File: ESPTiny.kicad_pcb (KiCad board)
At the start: 2 copper layers, 33 x 26.4 mm, 18 parts, among them J1 Conn_01x10_Male, J2 Conn_01x10_Male, J3 Conn_01x04_Male, U1 ESP-01v090, U2 ATtiny84-20PU, U3 MCP1700-3302E_TO92

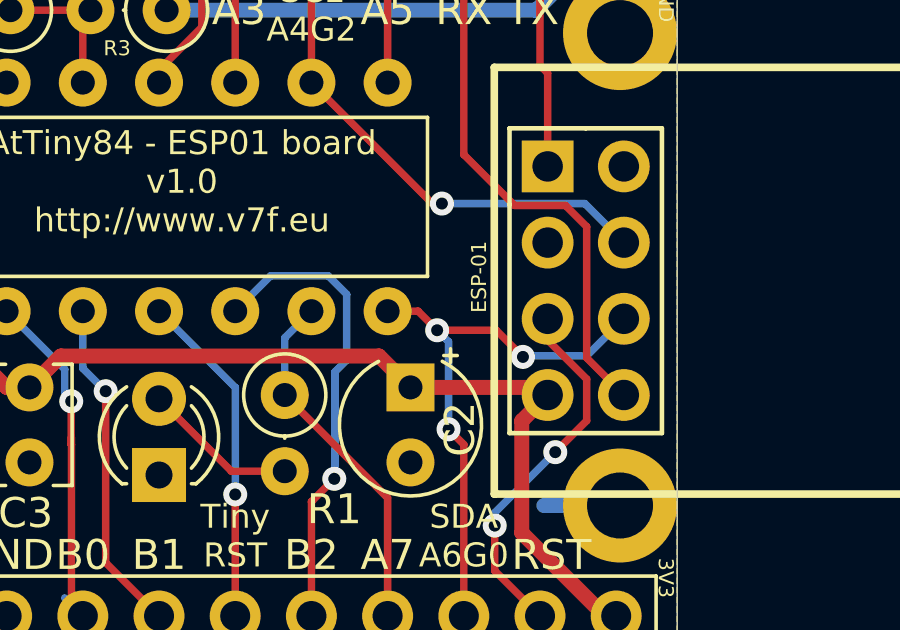
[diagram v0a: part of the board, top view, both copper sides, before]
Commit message: Fix ESP CH_PD to 3V3
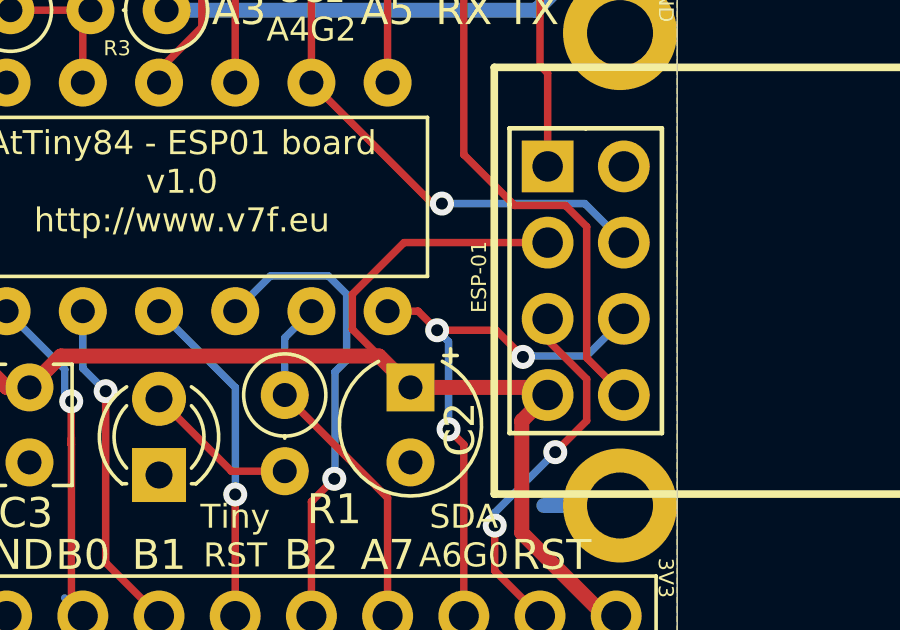
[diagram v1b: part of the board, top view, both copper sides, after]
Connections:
- U1 pad 3: GND -> +3V3
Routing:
- net +3V3: track 45.1 -> 56.2 mm

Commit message: Copper fill
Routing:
- net +3V3: track 56.2 -> 45.1 mm
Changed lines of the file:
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@@
     (thickness 1.6)
     (drawings 49)
-    (tracks 154)
+    (tracks 150)
     (zones 0)
     (modules 18)
@@
   (segment (start 43.942 61.722) (end 47.244 65.024) (width 0.5) (layer F.Cu) (net 2))
   (segment (start 43.942 60.706) (end 43.942 61.722) (width 0.5) (layer F.Cu) (net 2))
-  (segment (start 61.308999 55.466999) (end 63.246 57.404) (width 0.25) (layer F.Cu) (net 2))
-  (segment (start 61.308999 54.299999) (end 61.308999 55.466999) (width 0.25) (layer F.Cu) (net 2))
-  (segment (start 63.030998 52.578) (end 61.308999 54.299999) (width 0.25) (layer F.Cu) (net 2))
-  (segment (start 67.818 52.578) (end 63.030998 52.578) (width 0.25) (layer F.Cu) (net 2))
   (segment (start 43.528999 48.419001) (end 43.434 48.514) (width 0.25) (layer F.Cu) (net 3))
   (segment (start 43.022999 48.102999) (end 43.434 48.514) (width 0.5) (layer F.Cu) (net 3))
@@
   )
   (zone (net 2) (net_name +3V3) (layer F.Cu) (hatch edge 0.508)
+    (priority 1)
     (connect_pads (clearance 0.508))
     (min_thickness 0.254)

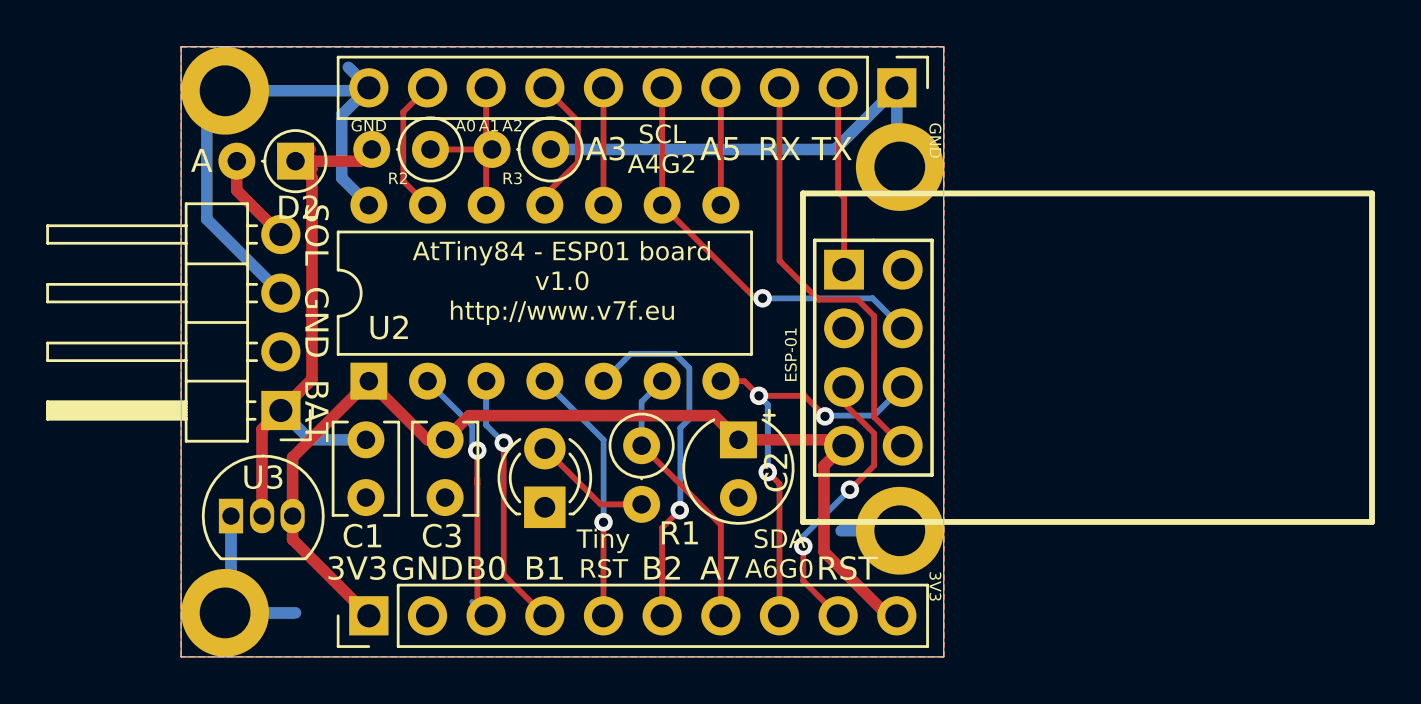
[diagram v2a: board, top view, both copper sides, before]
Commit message: Copper fill smaller clearance
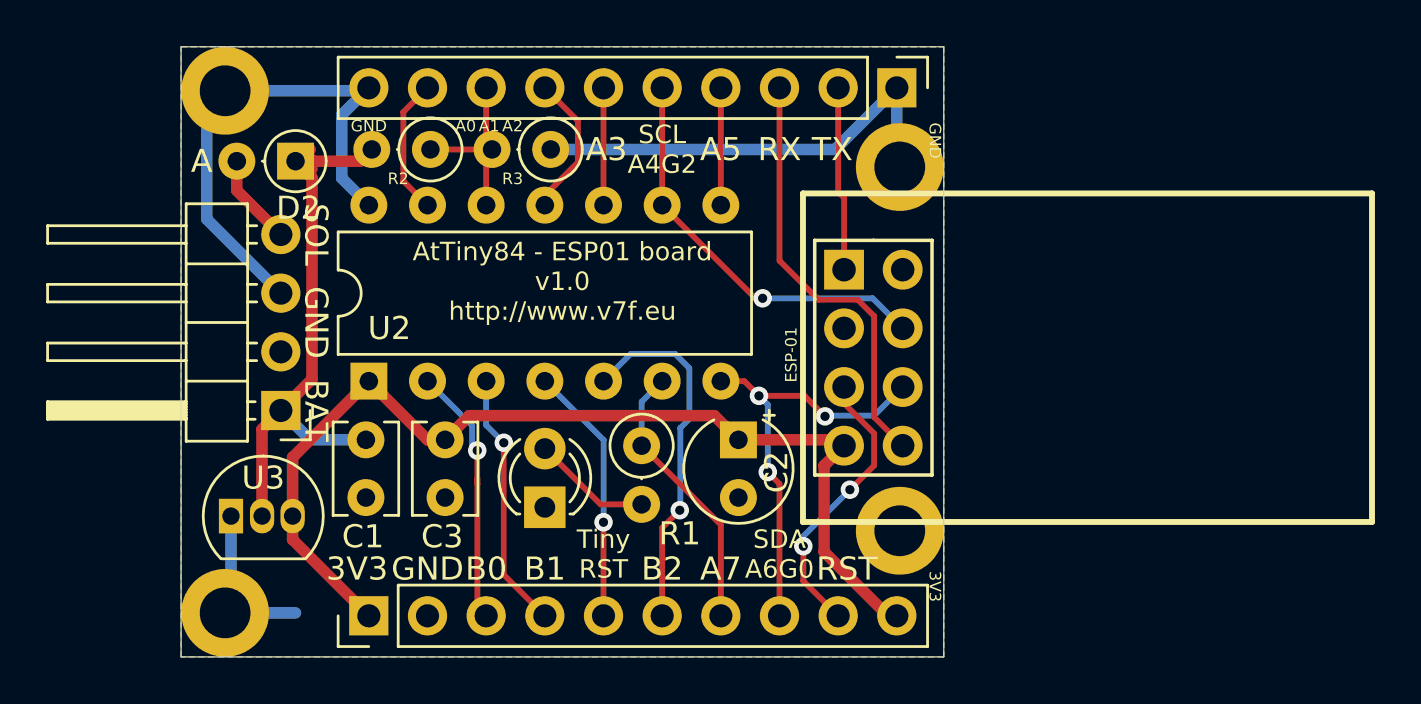
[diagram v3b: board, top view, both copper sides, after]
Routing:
- net GND: track 53.6 -> 49.8 mm
- net /B0: track 12.3 -> 11.4 mm
- removed copper zone on F.Cu, net (none)

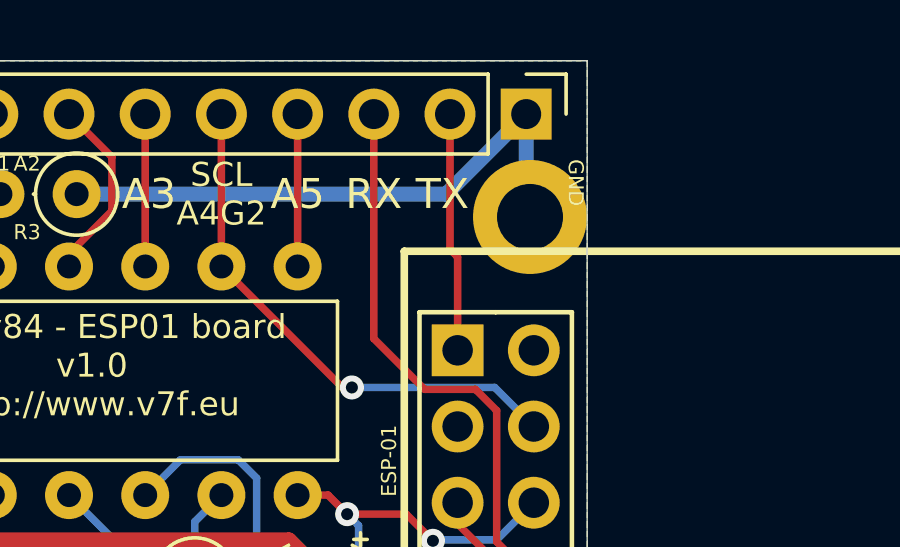
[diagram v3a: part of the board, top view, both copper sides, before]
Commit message: Copper fill smaller clearance: 0.27
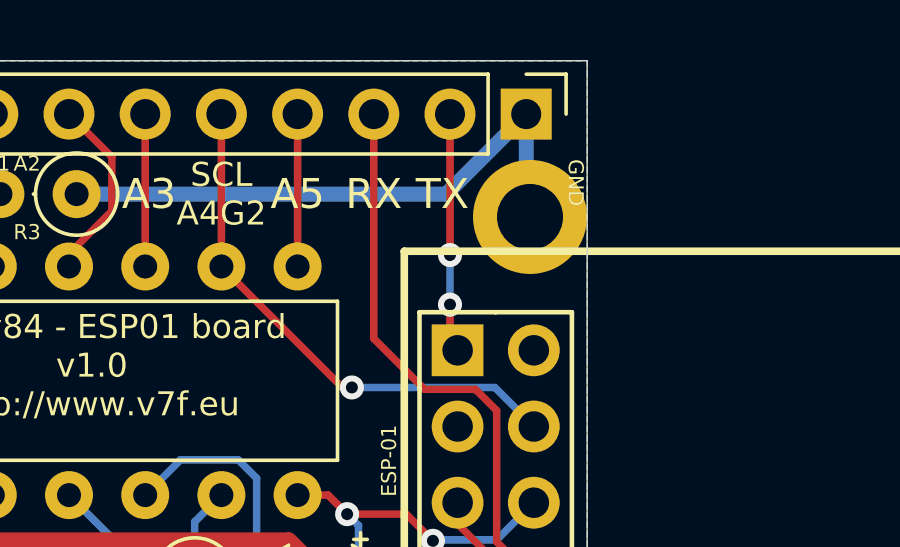
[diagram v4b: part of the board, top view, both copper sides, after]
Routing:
- net /TX: vias 0 -> 2
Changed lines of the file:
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@@
     (thickness 1.6)
     (drawings 49)
-    (tracks 147)
+    (tracks 150)
     (zones 0)
     (modules 18)
@@
     (last_trace_width 0.25)
     (trace_clearance 0.25)
-    (zone_clearance 0.29)
+    (zone_clearance 0.27)
     (zone_45_only no)
     (trace_min 0.25)
@@
   (segment (start 66.054401 61.580599) (end 66.054401 62.010167) (width 0.25) (layer B.Cu) (net 12))
   (segment (start 68.072 59.563) (end 66.054401 61.580599) (width 0.25) (layer B.Cu) (net 12))
-  (segment (start 67.564 46.674002) (end 67.564 42.164) (width 0.25) (layer F.Cu) (net 13) (status 20))
-  (segment (start 67.818 46.928002) (end 67.564 46.674002) (width 0.25) (layer F.Cu) (net 13))
-  (segment (start 67.818 50.038) (end 67.818 46.928002) (width 0.25) (layer F.Cu) (net 13) (status 10))
+  (via (at 67.564 46.863) (size 0.8) (drill 0.4) (layers F.Cu B.Cu) (net 13))
+  (via (at 67.564 48.514) (size 0.8) (drill 0.4) (layers F.Cu B.Cu) (net 13))
+  (segment (start 67.564 42.164) (end 67.564 46.863) (width 0.25) (layer F.Cu) (net 13))
+  (segment (start 67.564 49.784) (end 67.818 50.038) (width 0.25) (layer F.Cu) (net 13))
+  (segment (start 67.564 48.514) (end 67.564 49.784) (width 0.25) (layer F.Cu) (net 13))
+  (segment (start 67.564 46.863) (end 67.564 48.514) (width 0.25) (layer B.Cu) (net 13))
   (segment (start 69.119399 56.419399) (end 70.358 57.658) (width 0.25) (layer F.Cu) (net 14) (status 20))
   (segment (start 69.119399 52.046269) (end 69.119399 56.419399) (width 0.25) (layer F.Cu) (net 14))
@@
   (segment (start 49.784 47.244) (end 48.735999 46.195999) (width 0.25) (layer F.Cu) (net 20) (status 10))
   (zone (net 1) (net_name GND) (layer B.Cu) (hatch edge 0.508)
-    (connect_pads (clearance 0.29))
+    (connect_pads (clearance 0.27))
     (min_thickness 0.254)
     (fill yes (arc_segments 32) (thermal_gap 0.508) (thermal_bridge_width 0.508))
@@
   (zone (net 2) (net_name +3V3) (layer F.Cu) (hatch edge 0.508)
     (priority 1)
-    (connect_pads (clearance 0.28))
+    (connect_pads (clearance 0.27))
     (min_thickness 0.254)
     (fill yes (arc_segments 32) (thermal_gap 0.508) (thermal_bridge_width 0.508))
